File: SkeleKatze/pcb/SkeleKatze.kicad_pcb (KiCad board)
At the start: 2 copper layers, 116.3 x 78.3 mm, 6 parts, among them SW1 SW_SPDT

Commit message: rerouted tracks to LED2
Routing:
- net GND: track 75.9 -> 72.2 mm
- net Net-(D1-A): track 81.6 -> 80.1 mm
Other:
- board text added: "SkeleKatze R 1.0"
- board text removed: "SkeleCatze R 1.0"
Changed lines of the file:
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@@
 		(capping no)
 		(filling no)
+		(zone_defaults)
 		(pcbplotparams
 			(layerselection 0x00000000_00000000_55555555_575555ff)
@@
 		(layer "Edge.Cuts")
 	)
-	(gr_text "SkeleCatze\nR 1.0"
+	(gr_text "SkeleKatze\nR 1.0"
 		(at 104.4 40 0)
 		(layer "B.SilkS")
@@
 	)
 	(segment
-		(start 102.399997 77.473995)
-		(end 105 74.873992)
+		(start 102.8 44.4)
+		(end 102.8 44.3)
 		(width 0.3048)
 		(layer "B.Cu")
@@
 	)
 	(segment
-		(start 122.087738 35)
-		(end 124.751012 32.336726)
+		(start 102.399997 77.473995)
+		(end 105 74.873992)
 		(width 0.3048)
 		(layer "B.Cu")
@@
 	)
 	(segment
-		(start 105 68)
-		(end 94.2 57.2)
+		(start 102.8 44.3)
+		(end 109.2352 37.8648)
 		(width 0.3048)
 		(layer "B.Cu")
@@
 	)
 	(segment
-		(start 105 74.873992)
-		(end 105 68)
+		(start 119.222938 37.8648)
+		(end 124.751012 32.336726)
 		(width 0.3048)
 		(layer "B.Cu")
@@
 	)
 	(segment
-		(start 96.4 47.6)
-		(end 101.6 47.6)
+		(start 105 68)
+		(end 94.2 57.2)
 		(width 0.3048)
 		(layer "B.Cu")
@@
 	)
 	(segment
-		(start 102.8 38)
-		(end 105.8 35)
+		(start 105 74.873992)
+		(end 105 68)
 		(width 0.3048)
 		(layer "B.Cu")
@@
 	)
 	(segment
-		(start 102.8 44.4)
-		(end 102.8 38)
+		(start 96.4 47.6)
+		(end 101.6 47.6)
 		(width 0.3048)
 		(layer "B.Cu")
@@
 	)
 	(segment
-		(start 105.8 35)
-		(end 122.087738 35)
+		(start 109.2352 37.8648)
+		(end 119.222938 37.8648)
 		(width 0.3048)
 		(layer "B.Cu")
@@
 	)
 	(segment
-		(start 100.259999 39.740001)
-		(end 105.8 34.2)
-		(width 0.3048)
+		(start 94.15 72.65)
+		(end 100.4 66.4)
+		(width 0.2)
 		(layer "B.Cu")
 		(net "Net-(D1-A)")
 	)
 	(segment
-		(start 94.15 72.65)
-		(end 100.4 66.4)
+		(start 100.259999 42.4)
+		(end 105.199999 37.46)
 		(width 0.2)
 		(layer "B.Cu")
@@
 	(segment
 		(start 100.259999 44.4)
-		(end 100.259999 39.740001)
-		(width 0.3048)
+		(end 100.259999 42.4)
+		(width 0.2)
 		(layer "B.Cu")
 		(net "Net-(D1-A)")
@@
 	)
 	(segment
-		(start 105.8 34.2)
-		(end 119.512264 34.2)
-		(width 0.3048)
+		(start 105.199999 37.46)
+		(end 116.252264 37.46)
+		(width 0.2)
 		(layer "B.Cu")
 		(net "Net-(D1-A)")
 	)
 	(segment
-		(start 98.96021 44.4)
-		(end 100.259999 44.4)
+		(start 116.252264 37.46)
+		(end 122.448989 31.263275)
 		(width 0.2)
 		(layer "B.Cu")
@@
 	)
 	(segment
-		(start 119.512264 34.2)
-		(end 122.448989 31.263275)
-		(width 0.3048)
+		(start 98.96021 44.4)
+		(end 100.259999 44.4)
+		(width 0.2)
 		(layer "B.Cu")
 		(net "Net-(D1-A)")

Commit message: Final cut R 1.0
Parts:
- removed SW1: SW_SPDT, Button_Switch_SMD:SW_SPDT_PCM12
- added SW2: SW_Push, ZAM-Parts:SW_PUSH_SPST_ 1208Yd, B.Cu at (215.0, 87.3)
- Lg1: footprint SkeleKatze-Lib:SkeleKatze-Combined -> SkeleKatze-Lib:SkeleKatze-Merged
- moved Lg1 112.2 mm to (215.0, 77.2)
- moved BT1 110.9 mm to (209.3, 104.6), turned to 0 degrees
- moved D2 110.3 mm to (234.1, 47.0), turned to -115 degrees
- moved Lg2 109.6 mm to (207.1, 43.6)
- moved D1 108.1 mm to (209.8, 59.3), turned to -90 degrees
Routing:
- net Net-(D1-A): track 80.1 -> 64.0 mm
- net GND: track 72.2 -> 81.6 mm
- net Net-(BT1-+): track 40.0 -> 34.8 mm
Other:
- board size 116.3 x 78.3 mm -> 54.5 x 82.9 mm
- board text added: "Schrödingers Katze David Füleki R1.0"
- board text removed: "SkeleKatze R 1.0"

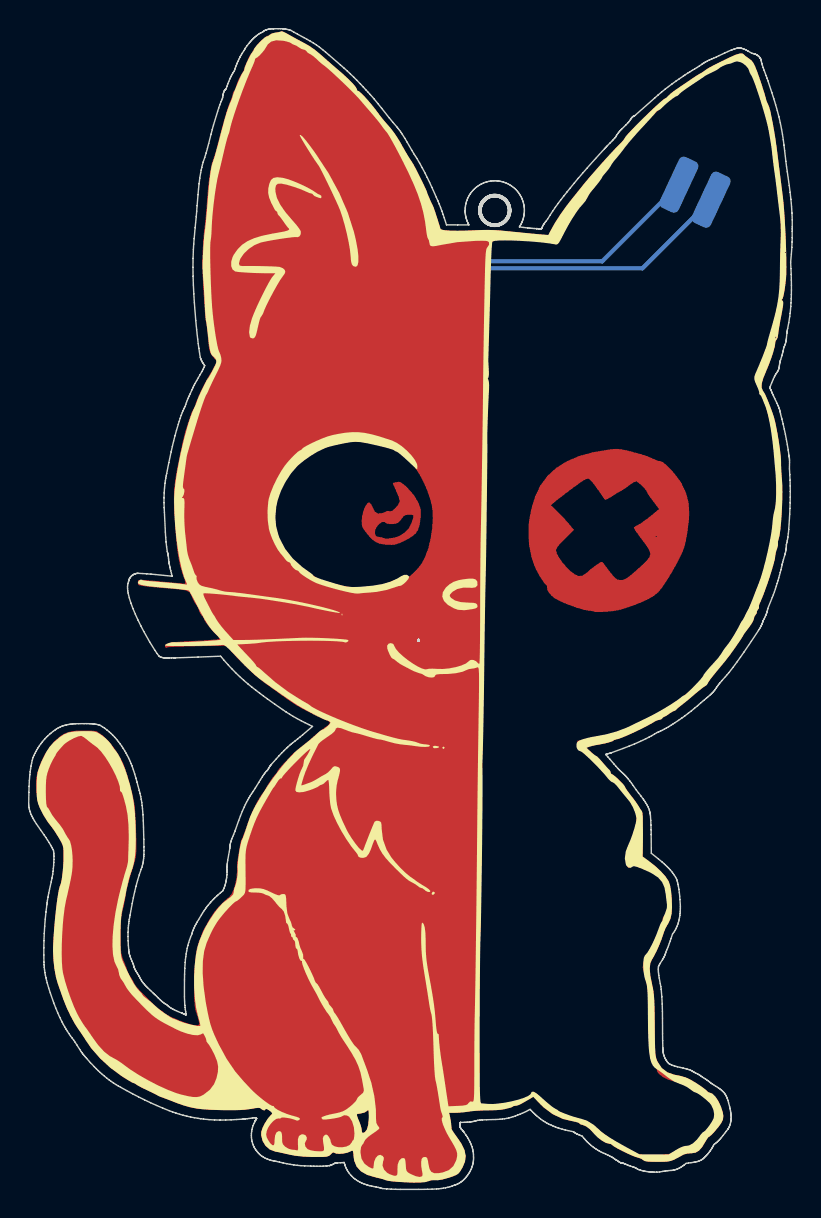
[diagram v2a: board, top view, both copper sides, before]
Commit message: Creates a Non-Front-Silkscreen version
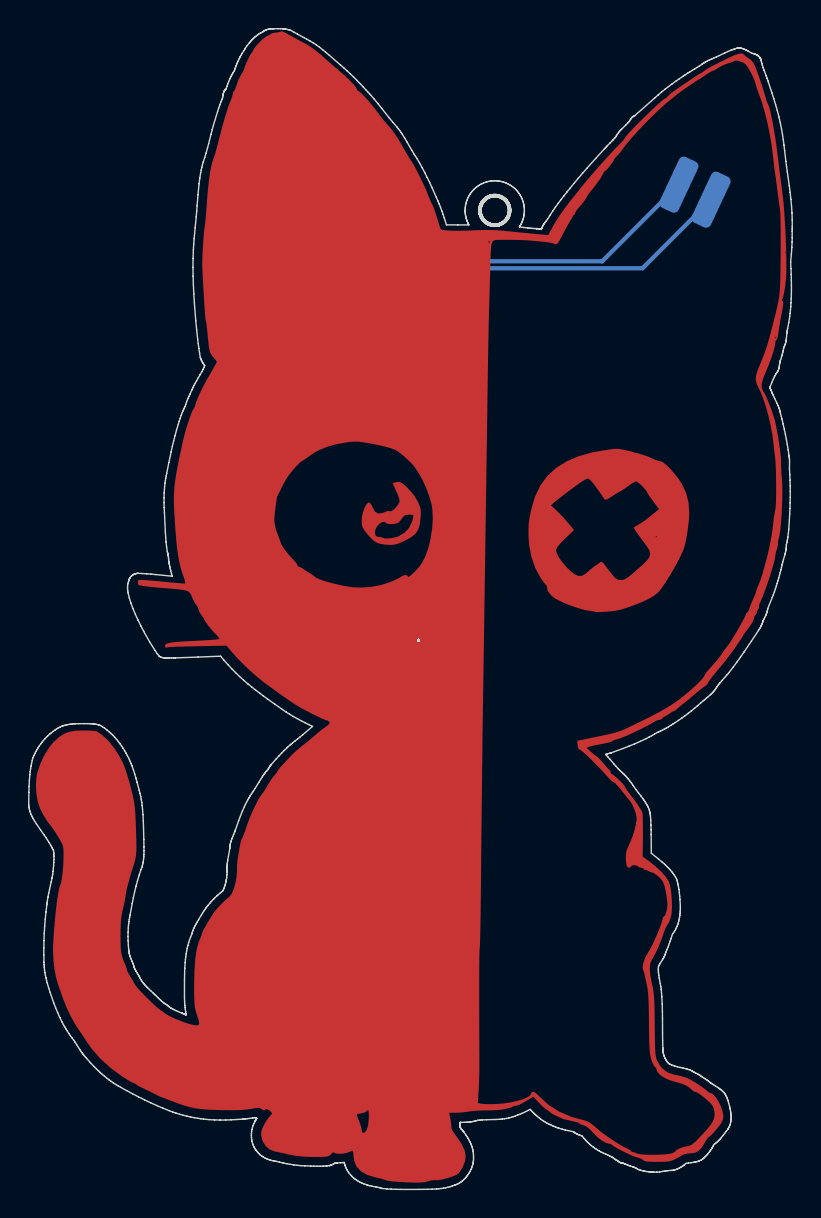
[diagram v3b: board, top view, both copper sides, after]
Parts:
- Lg1: footprint SkeleKatze-Lib:SkeleKatze-Merged -> SkeleKatze-Lib:SkeleKatze-Merged-NFS
